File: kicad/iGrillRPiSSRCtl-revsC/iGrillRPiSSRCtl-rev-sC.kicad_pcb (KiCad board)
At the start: 2 copper layers, 65 x 56 mm, 21 parts, among them J1 Conn_01x02, P1 Conn_02x20_Odd_Even

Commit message: Board updates
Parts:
- removed On    Off: SW_DPDT_x2, Button_Switch_THT:SW_CuK_JS202011CQN_DPDT_Straight
- added SW1: Off On, Button_Switch_THT:SW_CuK_JS202011CQN_DPDT_Straight, F.Cu at (71.0, 30.3)
- J1: footprint Connector_Wire:SolderWirePad_1x02_P3.81mm_Drill0.8mm -> TerminalBlock:TerminalBlock_bornier-2_P5.08mm
- moved REF** 6.37 mm to (54.8, 31.8)
- moved BZ1 3.25 mm to (75.3, 46.9)
- moved J1 3.16 mm to (78.0, 33.8)
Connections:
- J1 pad 2: /GPIO13(PWM1) -> /GPIO19(SPI1_MISO)
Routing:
- net /GPIO12(PWM0): track 15.2 -> 0.00 mm
- net /GPIO6: track 0.00 -> 11.9 mm
- net /GPIO19(SPI1_MISO): track 0.00 -> 11.9 mm
- net /GPIO13(PWM1): track 14.8 -> 10.3 mm
- net Net-(BZ1-Pad2): track 7.19 -> 10.8 mm

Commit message: footprint update
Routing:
- net /GPIO13(PWM1): track 10.3 -> 9.75 mm
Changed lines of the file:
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@@
-(kicad_pcb (version 20171130) (host pcbnew 5.1.2-f72e74a~84~ubuntu18.04.1)
+(kicad_pcb (version 20171130) (host pcbnew "(5.1.2)-2")
   (general
     (thickness 1.6)
     (drawings 36)
-    (tracks 30)
+    (tracks 33)
     (zones 0)
     (modules 21)
@@
   (segment (start 44.420001 21.180001) (end 25.829999 21.180001) (width 0.2) (layer F.Cu) (net 1))
   (segment (start 45.81 22.57) (end 44.420001 21.180001) (width 0.2) (layer F.Cu) (net 1) (status 10))
-  (segment (start 63.59 28.722) (end 67.677 32.809) (width 0.2) (layer F.Cu) (net 7))
-  (segment (start 63.59 22.57) (end 63.59 28.722) (width 0.2) (layer F.Cu) (net 7))
+  (segment (start 66.977001 32.109001) (end 67.677 32.809) (width 0.2) (layer F.Cu) (net 7))
+  (segment (start 65.88038 31.01238) (end 66.977001 32.109001) (width 0.2) (layer F.Cu) (net 7))
+  (segment (start 65.88038 24.85674) (end 65.88038 31.01238) (width 0.2) (layer F.Cu) (net 7))
+  (segment (start 64.443639 23.419999) (end 65.88038 24.85674) (width 0.2) (layer F.Cu) (net 7))
+  (segment (start 63.59 22.57) (end 64.439999 23.419999) (width 0.2) (layer F.Cu) (net 7))
+  (segment (start 64.439999 23.419999) (end 64.443639 23.419999) (width 0.2) (layer F.Cu) (net 7))
   (segment (start 18 48.5) (end 20 50.5) (width 0.2) (layer F.Cu) (net 9) (status 20))
   (segment (start 18 26) (end 18 48.5) (width 0.2) (layer F.Cu) (net 9))
@@
   (segment (start 30.57 22.57) (end 28.14 25) (width 0.2) (layer F.Cu) (net 10) (status 10))
   (segment (start 28.14 25) (end 20 25) (width 0.2) (layer F.Cu) (net 10))
-  (segment (start 70.077 30.309) (end 70.977 30.309) (width 0.2) (layer F.Cu) (net 19))
-  (segment (start 66.13 26.362) (end 70.077 30.309) (width 0.2) (layer F.Cu) (net 19))
-  (segment (start 66.13 22.57) (end 66.13 26.362) (width 0.2) (layer F.Cu) (net 19))
-  (segment (start 74.77 28.67) (end 78 28.67) (width 0.2) (layer F.Cu) (net 20))
-  (segment (start 68.67 22.57) (end 74.77 28.67) (width 0.2) (layer F.Cu) (net 20))
+  (segment (start 70.977 27.417) (end 66.13 22.57) (width 0.2) (layer F.Cu) (net 19))
+  (segment (start 70.977 30.309) (end 70.977 27.417) (width 0.2) (layer F.Cu) (net 19))
+  (segment (start 74.77 28.67) (end 68.67 22.57) (width 0.2) (layer F.Cu) (net 20))
+  (segment (start 78 28.67) (end 74.77 28.67) (width 0.2) (layer F.Cu) (net 20))
   (segment (start 32.741 57.968) (end 31.09 56.317) (width 0.2) (layer F.Cu) (net 21))
   (segment (start 32.741 59.068) (end 32.741 57.968) (width 0.2) (layer F.Cu) (net 21))

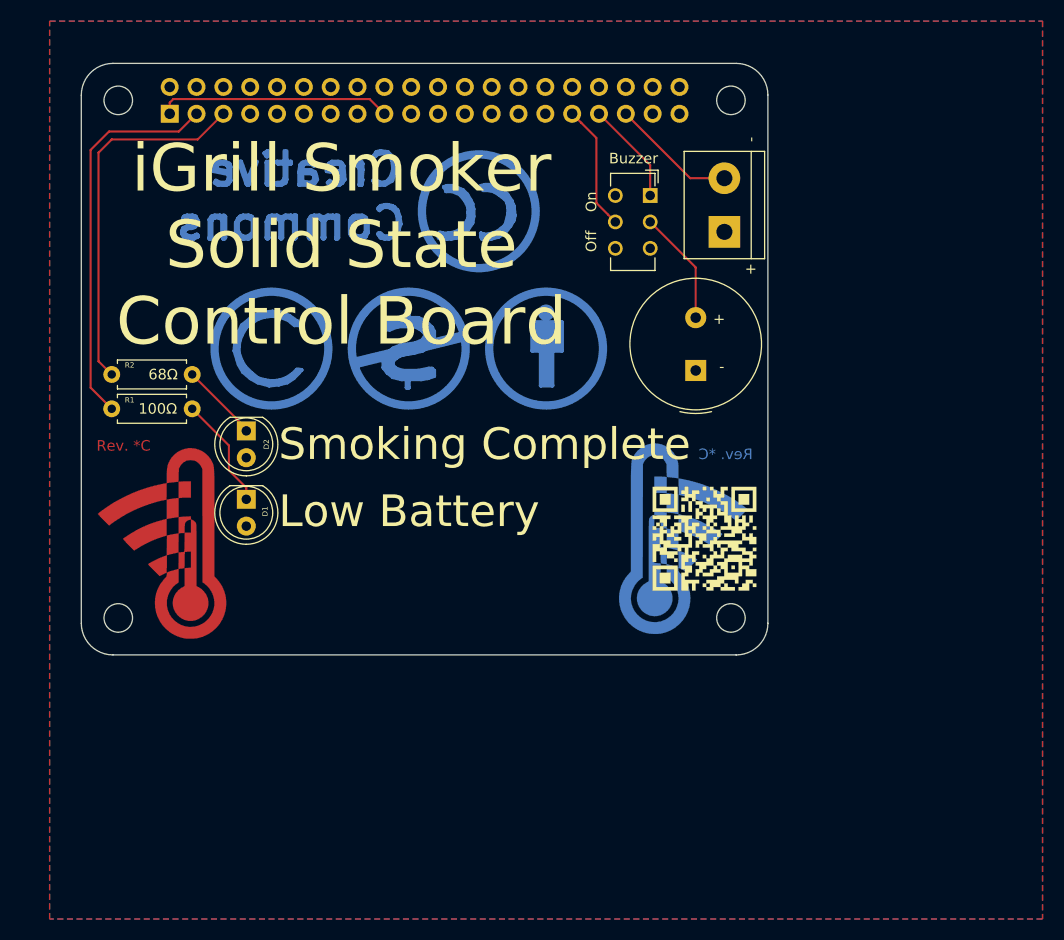
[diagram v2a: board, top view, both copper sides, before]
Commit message: Fixing pinout for RPi PWMs
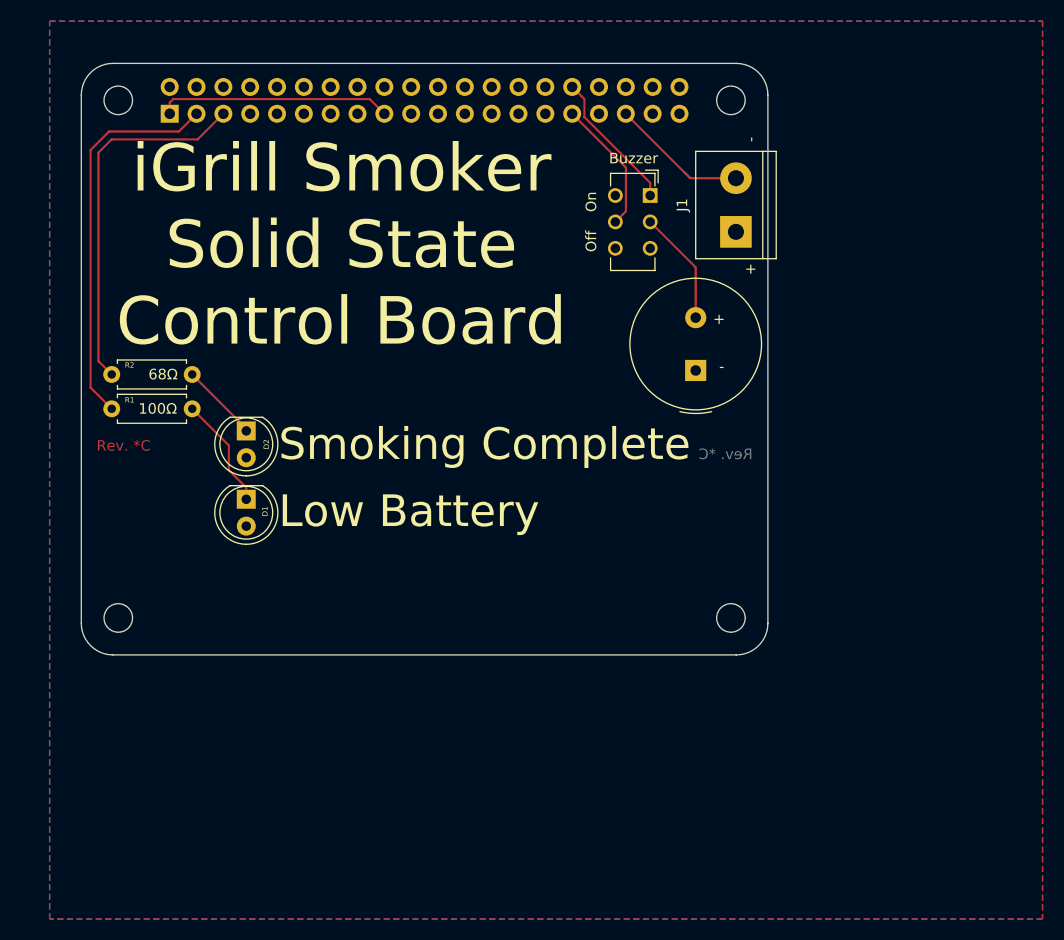
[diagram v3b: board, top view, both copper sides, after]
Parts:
- removed BackLogo, G***: LOGO, iGrillRPiSSRCtl-rev-sC:WiFiThem_18x12
- removed G*** (x2): LOGO, iGrillRPiSSRCtl-rev-sC:qr-code-12x12
- removed REF**: WEEE-Logo_5.6x8mm_SilkScreen, Symbol:WEEE-Logo_5.6x8mm_SilkScreen
- removed REF**: Symbol_CC-ShareAlike_CopperTop_Big, Symbol:Symbol_CC-ShareAlike_CopperTop_Big
- removed REF**: Symbol_CC-Noncommercial_CopperTop_Big, Symbol:Symbol_CC-Noncommercial_CopperTop_Big
- removed REF**: Symbol_CC-Attribution_CopperTop_Big, Symbol:Symbol_CC-Attribution_CopperTop_Big
- removed REF**: Symbol_CreativeCommons_CopperTop_Type1_Big, Symbol:Symbol_CreativeCommons_CopperTop_Type1_Big
- J1: value Conn_01x02 -> Screw_Terminal_01x02
- moved J1 1.10 mm to (79.1, 33.7)
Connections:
- SW1 pad 1: /GPIO13(PWM1) -> /GPIO12(PWM0)
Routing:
- net /GPIO12(PWM0): track 0.00 -> 13.3 mm
- net /GPIO13(PWM1): track 9.75 -> 0.00 mm
- net /GPIO19(SPI1_MISO): track 11.9 -> 13.7 mm
- net /GPIO6: track 11.9 -> 12.8 mm

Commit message: Updated design to fix issues from protoype
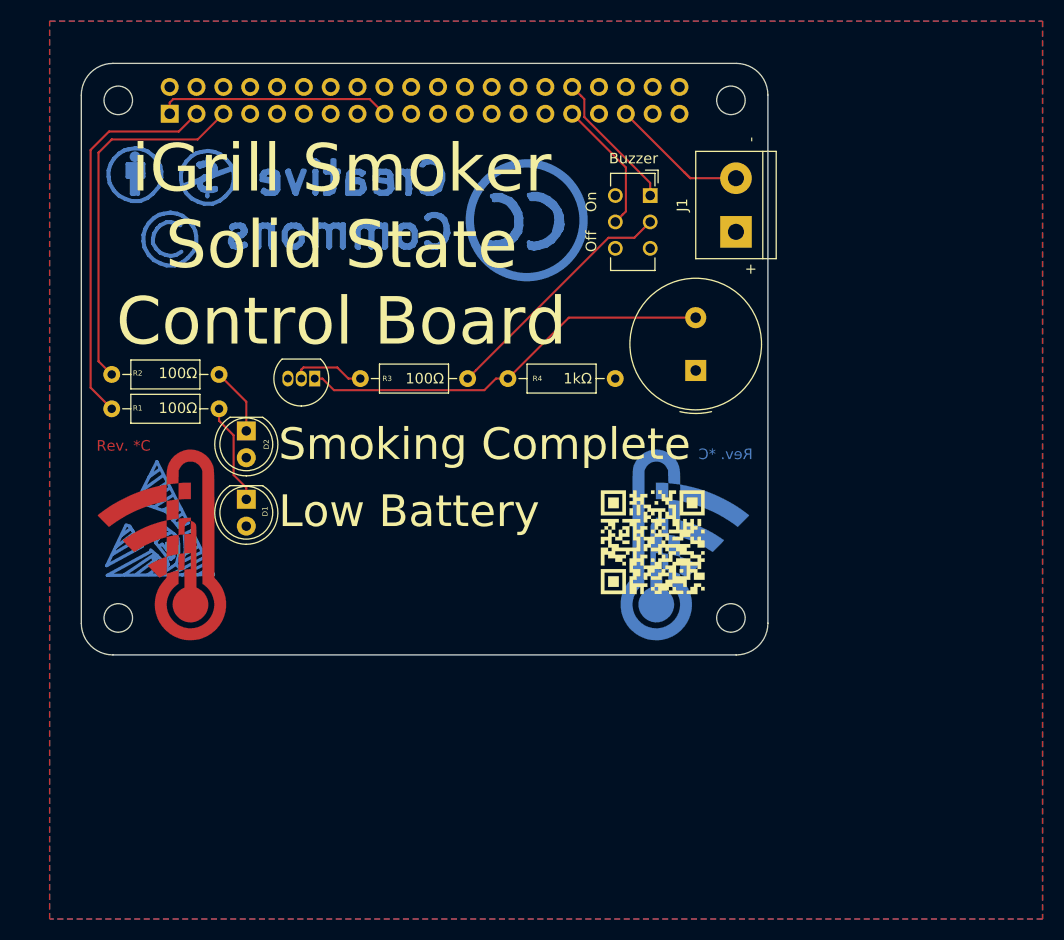
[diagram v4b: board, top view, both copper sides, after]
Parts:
- added G***: LOGO, iGrillRPiSSRCtl-rev-sC:qr-code-12x12, B.Cu at (48.1, 55.5)
- added G***: LOGO, iGrillRPiSSRCtl-rev-sC:qr-code-12x12, F.Cu at (71.2, 63.1)
- added G***: LOGO, iGrillRPiSSRCtl-rev-sC:WiFiThem_18x12, B.Cu at (74.3, 63.4)
- added G***: LOGO, iGrillRPiSSRCtl-rev-sC:WiFiThem_18x12, F.Cu at (24.7, 63.4)
- added Q1: Q_NPN_CBE, Package_TO_SOT_THT:TO-92_Inline, F.Cu at (39.2, 47.6)
- added R3: 100Ω, Resistor_THT:R_Axial_DIN0207_L6.3mm_D2.5mm_P10.16mm_Horizontal, F.Cu at (43.5, 47.6)
- added R4: 1kΩ, Resistor_THT:R_Axial_DIN0207_L6.3mm_D2.5mm_P10.16mm_Horizontal, F.Cu at (67.7, 47.6)
- added REF**: Symbol_ESD-Logo_CopperTop, Symbol:Symbol_ESD-Logo_CopperTop, B.Cu at (24.5, 62.9)
- added REF**: WEEE-Logo_8.4x12mm_SilkScreen, Symbol:WEEE-Logo_8.4x12mm_SilkScreen, B.Cu at (25.2, 43.6)
- added REF**: Symbol_CC-ShareAlike_CopperTop_Small, Symbol:Symbol_CC-ShareAlike_CopperTop_Small, B.Cu at (25.5, 34.4)
- added REF**: Symbol_CC-Attribution_CopperTop_Small, Symbol:Symbol_CC-Attribution_CopperTop_Small, B.Cu at (22.2, 28.3)
- added REF**: Symbol_CC-Noncommercial_CopperTop_Small, Symbol:Symbol_CC-Noncommercial_CopperTop_Small, B.Cu at (29.1, 28.6)
- added REF**: Symbol_CreativeCommons_CopperTop_Type1_Big, Symbol:Symbol_CreativeCommons_CopperTop_Type1_Big, B.Cu at (59.3, 32.7)
- R1: footprint Resistor_THT:R_Axial_DIN0207_L6.3mm_D2.5mm_P7.62mm_Horizontal -> Resistor_THT:R_Axial_DIN0207_L6.3mm_D2.5mm_P10.16mm_Horizontal
- R2: value 68Ω -> 100Ω; footprint Resistor_THT:R_Axial_DIN0207_L6.3mm_D2.5mm_P7.62mm_Horizontal -> Resistor_THT:R_Axial_DIN0207_L6.3mm_D2.5mm_P10.16mm_Horizontal
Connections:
- SW1 pad 2: Net-(BZ1-Pad2) -> Net-(R3-Pad2)
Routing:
- net Net-(BZ1-Pad2): track 10.8 -> 39.4 mm
- net Net-(R3-Pad2): track 0.00 -> 23.4 mm
- net Net-(Q1-Pad2): track 0.00 -> 6.96 mm
- net Net-(D1-Pad1): track 10.7 -> 9.64 mm
- net Net-(D2-Pad1): track 7.81 -> 6.98 mm

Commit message: Updates from protoype **
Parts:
- added Q2: Q_PNP_BCE, Package_TO_SOT_THT:TO-92_Inline, F.Cu at (20.4, 51.2)
- added Q3: Q_PNP_BCE, Package_TO_SOT_THT:TO-92_Inline, F.Cu at (20.2, 45.6)
- moved REF** 29.8 mm to (52.0, 56.6)
- moved G*** 13.9 mm to (62.0, 55.5)
- moved R1 13.8 mm to (33.8, 49.4), turned to 180 degrees
- moved R2 13.8 mm to (33.8, 46.4), turned to 180 degrees
- moved D1 3.00 mm to (32.8, 62.1), turned to 90 degrees
- moved D2 2.98 mm to (32.8, 55.6), turned to 90 degrees
- moved Q1 1.16 mm to (39.2, 48.8), turned to 90 degrees
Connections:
- D1 pad 1: Net-(D1-Pad1) -> GND
- D1 pad 2: +5V -> Net-(D1-Pad2)
- D2 pad 1: Net-(D2-Pad1) -> GND
- D2 pad 2: +5V -> Net-(D2-Pad2)
- J1 pad 2: /GPIO19(SPI1_MISO) -> /GPIO13(PWM1)
- R1 pad 1: /GPIO2(SDA1) -> Net-(D1-Pad2)
- R1 pad 2: Net-(D1-Pad1) -> Net-(Q2-Pad2)
- R2 pad 1: /GPIO3(SCL1) -> Net-(D2-Pad2)
- R2 pad 2: Net-(D2-Pad1) -> Net-(Q3-Pad2)
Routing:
- net /GPIO13(PWM1): track 0.00 -> 15.5 mm
- net /GPIO19(SPI1_MISO): track 13.7 -> 0.00 mm
- net Net-(D1-Pad2): track 0.00 -> 10.7 mm
- net Net-(D1-Pad1): track 9.64 -> 0.00 mm
- net Net-(D2-Pad2): track 0.00 -> 8.36 mm
- net Net-(D2-Pad1): track 6.98 -> 0.00 mm
- net Net-(Q3-Pad2): track 0.00 -> 4.26 mm
- net Net-(Q2-Pad2): track 0.00 -> 3.42 mm
- net Net-(Q1-Pad2): track 6.96 -> 4.36 mm
- net /GPIO3(SCL1): track 34.9 -> 33.4 mm
- net /GPIO2(SDA1): track 36.8 -> 38.2 mm
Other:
- board text added: "02 - Red LED 03 - Green LED 06 - Switch 12 - Buzzer 13 - SSR (J1)"
- board text added: "B C E"
- board text added: "BCM - Function"
- board text added: "C B E"
- board text added: "NPN"
- board text added: "PNP"

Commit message: Updating board design
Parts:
- Q1: value Q_NPN_CBE -> Q_NPN_ECB; footprint Package_TO_SOT_THT:TO-92_Inline -> Package_TO_SOT_THT:TO-92_Inline_Wide
- Q2, Q3: value Q_PNP_BCE -> Q_PNP_EBC; footprint Package_TO_SOT_THT:TO-92_Inline -> Package_TO_SOT_THT:TO-92_Inline_Wide
- moved Q1 3.70 mm to (39.2, 45.1), turned to 270 degrees
- moved Q3 1.48 mm to (20.4, 44.1)
- moved Q2 0.50 mm to (20.4, 51.7)
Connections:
- Q1 pad 1: Net-(BZ1-Pad2) -> GND
- Q1 pad 3: GND -> Net-(BZ1-Pad2)
- Q2 pad 1: /GPIO2(SDA1) -> +5V
- Q2 pad 2: Net-(Q2-Pad2) -> /GPIO2(SDA1)
- Q2 pad 3: +5V -> Net-(Q2-Pad3)
- Q3 pad 1: /GPIO3(SCL1) -> +5V
- Q3 pad 2: Net-(Q3-Pad2) -> /GPIO3(SCL1)
- Q3 pad 3: +5V -> Net-(Q3-Pad3)
- R1 pad 2: Net-(Q2-Pad2) -> Net-(Q2-Pad3)
- R2 pad 2: Net-(Q3-Pad2) -> Net-(Q3-Pad3)
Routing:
- net Net-(Q3-Pad3): track 0.00 -> 10.2 mm
- net Net-(Q2-Pad3): track 0.00 -> 4.38 mm
- net Net-(Q3-Pad2): track 4.26 -> 0.00 mm
- net /GPIO3(SCL1): track 33.4 -> 29.4 mm
- net Net-(Q2-Pad2): track 3.42 -> 0.00 mm
- net Net-(R3-Pad2): track 23.4 -> 26.8 mm
- net /GPIO2(SDA1): track 38.2 -> 35.6 mm
- net /GPIO6: track 12.8 -> 13.7 mm
- net Net-(D1-Pad2): track 10.7 -> 11.4 mm
- net Net-(BZ1-Pad2): track 38.9 -> 39.5 mm
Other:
- board text added: "E B C"
- board text removed: "C B E"

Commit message: Cleanup and fixes
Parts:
- G*** (x2): footprint iGrillRPiSSRCtl-rev-sC:qr-code-12x12 -> iGrillRPiSSRCtl-rev-sC:qr-code-10x10_inverted
- Q2, Q3: value Q_PNP_EBC -> Q_NPN_ECB
- R4: value 1kΩ -> 1000Ω
- moved D1 2.73 mm to (32.7, 59.3), turned to 270 degrees
- moved D2 2.68 mm to (32.6, 52.9), turned to 270 degrees
- moved Q2 0.05 mm to (20.4, 51.8)
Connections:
- D1 pad 1: GND -> Net-(D1-Pad1)
- D1 pad 2: Net-(D1-Pad2) -> +5V
- D2 pad 1: GND -> Net-(D2-Pad1)
- D2 pad 2: Net-(D2-Pad2) -> +5V
- Q2 pad 1: +5V -> GND
- Q3 pad 1: +5V -> GND
- R1 pad 1: Net-(D1-Pad2) -> Net-(D1-Pad1)
- R2 pad 1: Net-(D2-Pad2) -> Net-(D2-Pad1)
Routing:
- net Net-(D1-Pad2): track 11.4 -> 0.00 mm
- net Net-(D1-Pad1): track 0.00 -> 11.4 mm
- net Net-(D2-Pad2): track 8.36 -> 0.00 mm
- net Net-(D2-Pad1): track 0.00 -> 7.79 mm
- net +3V3: track 22.1 -> 21.4 mm
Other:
- board text added: "RPi iGrill Smoker Solid State Relay Control Board"
- board text removed: "PNP"
- board text removed: "iGrill Smoker Solid State Control Board"
